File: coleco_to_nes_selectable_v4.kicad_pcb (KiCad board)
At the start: 2 copper layers, 113 x 42.5 mm, 24 parts, among them J1 Conn_01x09_Male, SW1 SW_DIP_x04

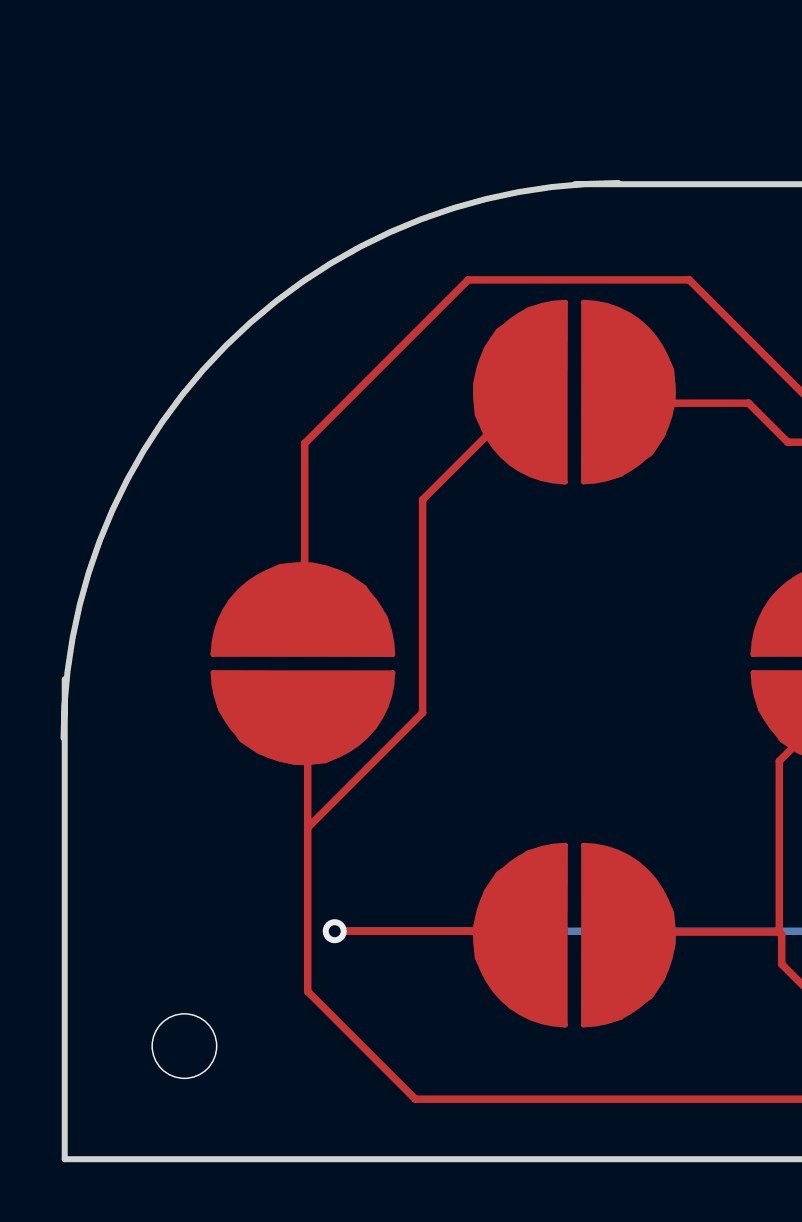
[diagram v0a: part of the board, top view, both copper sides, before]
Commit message: Fix "edge not closed" warnings on PCB
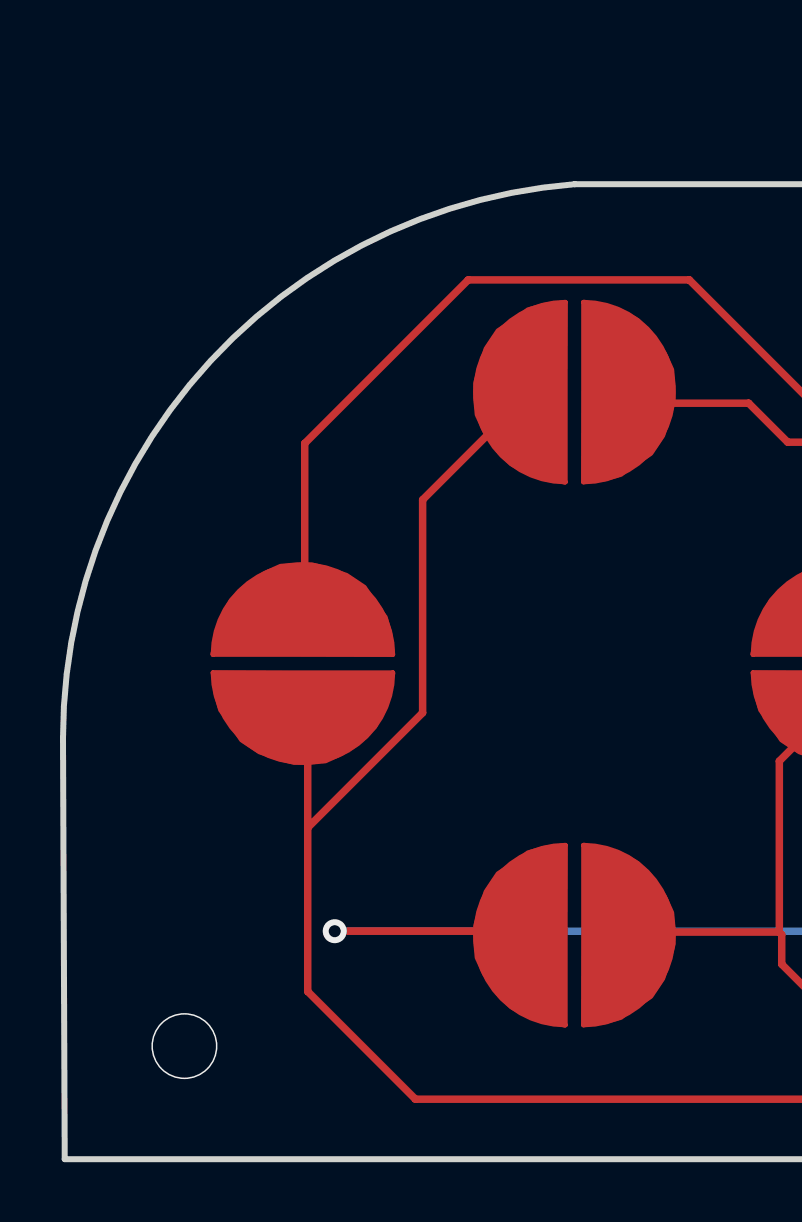
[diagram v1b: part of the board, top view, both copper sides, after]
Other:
- board size 113 x 42.5 mm -> 113.1 x 42.5 mm
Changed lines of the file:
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@@
-(kicad_pcb (version 20171130) (host pcbnew 5.0.2-5.fc29)
+(kicad_pcb (version 20171130) (host pcbnew "(5.1.5-0-10_14)")
   (general
     (thickness 1.6)
@@
     (zone_45_only no)
     (trace_min 0.2)
-    (segment_width 0.2)
-    (edge_width 0.2)
     (via_size 0.8)
     (via_drill 0.4)
@@
     (uvia_min_size 0.2)
     (uvia_min_drill 0.1)
+    (edge_width 0.2)
+    (segment_width 0.2)
     (pcb_text_width 0.3)
     (pcb_text_size 1.5 1.5)
@@
       (drillshape 0)
       (scaleselection 1)
-      (outputdirectory "coleco_to_nes_selectable_v4_gerbers/"))
+      (outputdirectory "coleco-to-nes-v4"))
   )
   (net 0 "")
@@
       (xy 0.09525 -0.485775)) (layer F.SilkS) (width 0.01))
   )
+  (gr_line (start 87.01 100.02) (end 86.952354 85.98) (layer Edge.Cuts) (width 0.2))
   (gr_line (start 120.01 67.52) (end 104.01 67.52) (layer Edge.Cuts) (width 0.2))
-  (gr_line (start 87.01 100.02) (end 87.01 84.02) (layer Edge.Cuts) (width 0.2))
   (gr_line (start 122.01 100.02) (end 87.01 100.02) (layer Edge.Cuts) (width 0.2))
   (gr_line (start 122.01 98.02) (end 122.01 100.02) (layer Edge.Cuts) (width 0.2))
@@
     (effects (font (size 1.5 1.5) (thickness 0.3)))
   )
-  (gr_arc (start 105.47 85.98) (end 105.47 67.48) (angle -90) (layer Edge.Cuts) (width 0.2))
+  (gr_arc (start 105.47 85.98) (end 104.01 67.52) (angle -85.47789438) (layer Edge.Cuts) (width 0.2))
   (via (at 91 96.25) (size 2.2) (drill 2.1) (layers F.Cu B.Cu) (net 0))
   (via (at 196 96.25) (size 2.2) (drill 2.1) (layers F.Cu B.Cu) (net 0))
